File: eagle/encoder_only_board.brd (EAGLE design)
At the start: 34.5 x 29.1 mm, 27 parts, among them IC2 AT42QT1010SOT23, J1 FH12-6S-0.5SH(55), J2 FH12-6S-0.5SH(55)

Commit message: Update switch voltage divider and connect encoder touch to it
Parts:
- added R6: 0, rcl:R0603
- R24: value 0 -> 10k
- R4: value 10k -> 100k
- moved R4 16.3 mm to (26.2, 2.51), turned to 270 degrees
- moved R3 12.2 mm to (24.2, 2.51)
- moved R1 4.06 mm to (14.0, 2.51)
- moved R2 4.06 mm to (9.93, 2.51)
- moved R23 4.06 mm to (22.1, 2.51)
- moved R27 4.06 mm to (18.1, 2.51)
- moved R28 4.06 mm to (20.1, 2.51)
- moved R36 4.06 mm to (16.0, 2.51)
- moved R5 4.06 mm to (12.0, 2.51)
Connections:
- removed net N$2: R2.2, R3.2, R4.1
- removed net SW1: J1.1, J2.6, R24.2, R27.2, R28.2
- new net SW_IN: J1.1, R27.2, R28.2, R6.1
- new net SW_OUT: J2.6, R3.2
- net ENC_SW: now also R3.1, R4.1
- net ENC_SW_PU: now also R24.2, R6.2; no longer R3.1
- net GND: now also R2.2
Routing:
- net SW1: track 69.6 -> 0.00 mm, vias 4 -> 0
- net SW_IN: track 0.00 -> 47.0 mm, vias 0 -> 3
- net SW_OUT: track 0.00 -> 15.1 mm
- net ENC_SW: track 5.72 -> 10.0 mm
- net N$2: track 4.06 -> 0.00 mm
- net VCC: track 98.0 -> 102.1 mm
- net POT+: track 6.83 -> 3.51 mm
- net ENC2B: track 47.6 -> 46.4 mm
- net POT: track 5.26 -> 4.43 mm
- net ENC2A: track 53.1 -> 52.4 mm
- net GND: vias 17 -> 26
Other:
- board text added: "E+T"
- board text added: "SWO"
- board text added: "v1.0.1"
- board text removed: "P+T"
- board text removed: "SW1,2"
- board text removed: "v1.0.0"

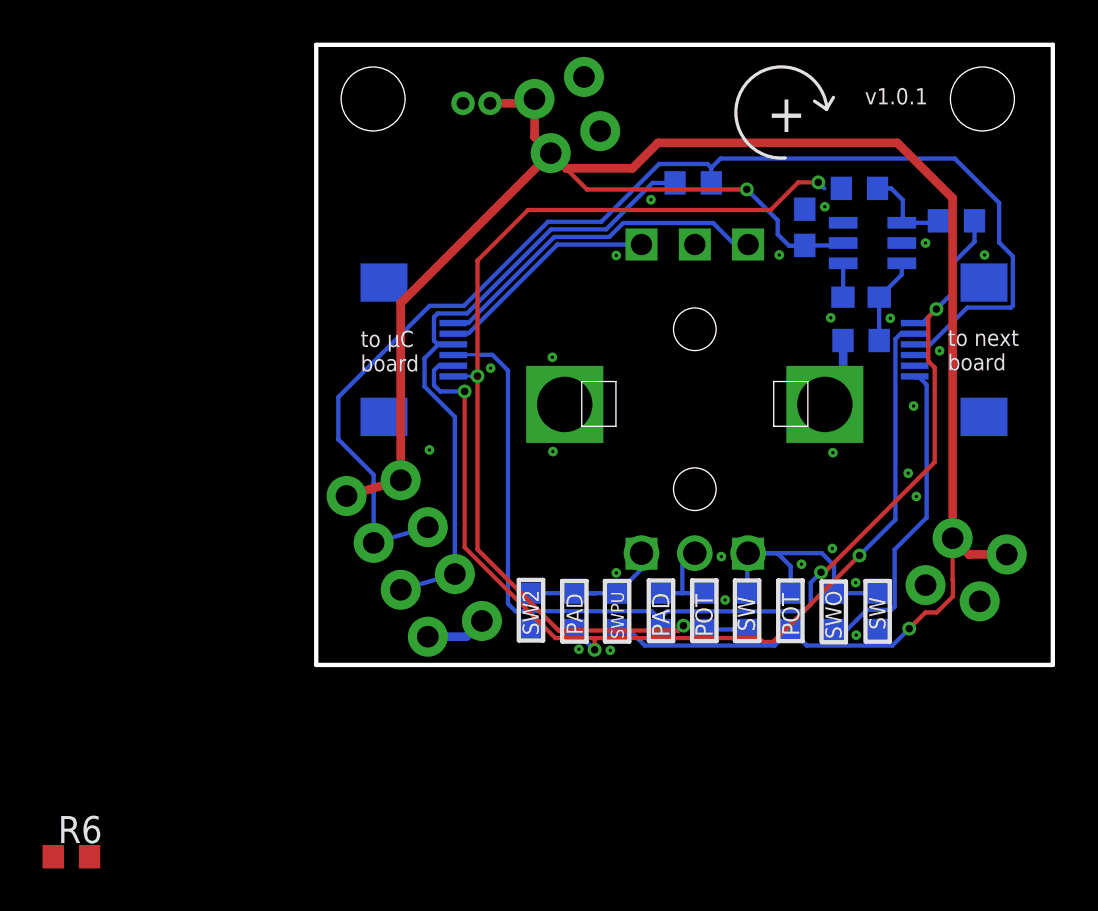
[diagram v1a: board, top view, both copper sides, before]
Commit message: Board version 4 WIP;
* Added solder pads to FFC connectors
* Fixed naming of connectors (previously M was on the right and labels
  were wrong
* Flipped builtin led (D1) around to make it safer to use with encoders
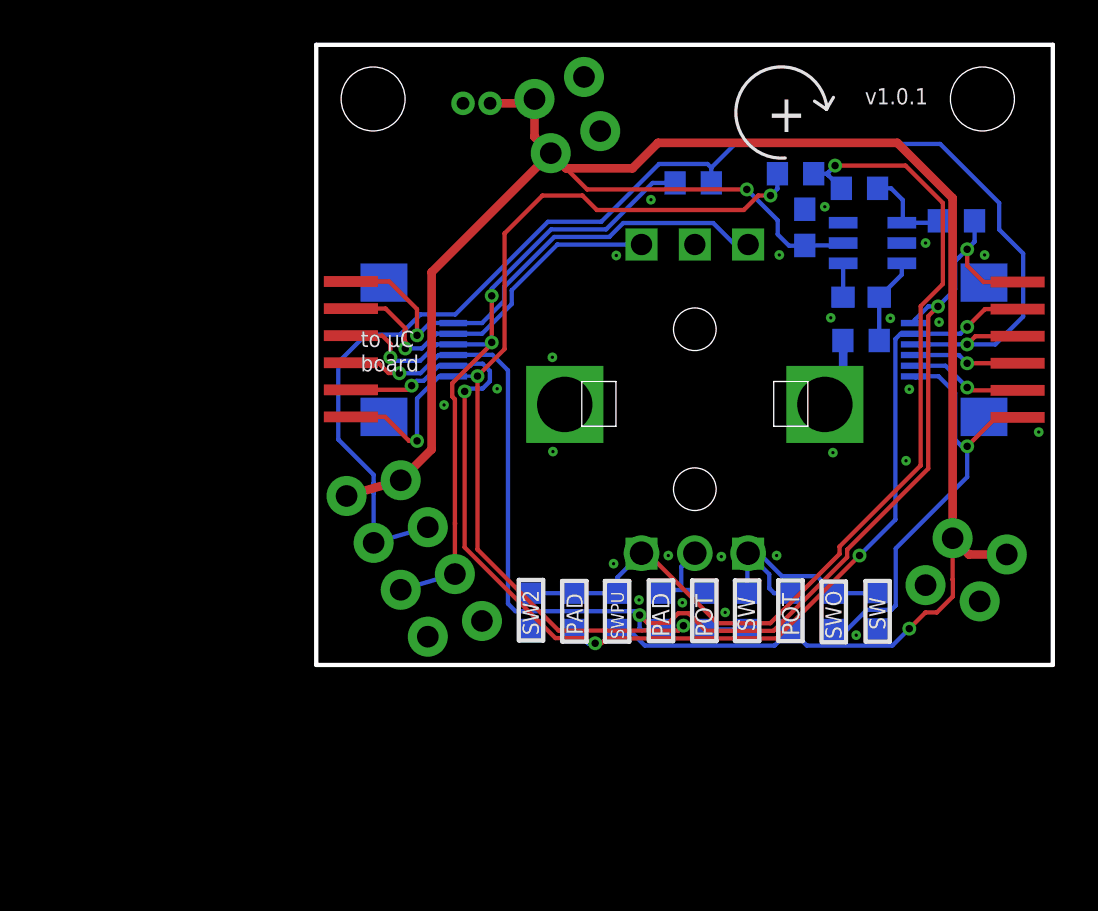
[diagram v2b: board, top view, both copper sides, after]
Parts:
- added U$1, U$2: 6PIN_SOLDER_PAD, edge:6PIN_SOLDER_PAD
- moved R6 46.7 mm to (22.4, 23.0), flipped to the bottom, turned to 180 degrees
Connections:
- removed net N$10: J2.4
- removed net N$14: J2.5
- new net NC1: J2.4, U$1.P$4
- new net NC2: J2.5, U$1.P$5
- net ENC1A: now also U$2.P$6
- net ENC1B: now also U$2.P$5
- net ENC2A: now also U$1.P$1, U$2.P$3
- net ENC2B: now also U$1.P$2, U$2.P$2
- net LED_IN: now also U$2.P$4
- net LED_OUT: now also U$1.P$3
- net SW_IN: now also U$2.P$1
- net SW_OUT: now also U$1.P$6
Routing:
- net ENC_SW_PU: track 7.48 -> 44.8 mm, vias 0 -> 1
- net ENC2B: track 46.4 -> 56.9 mm, vias 3 -> 5
- net ENC2A: track 52.4 -> 62.3 mm, vias 2 -> 4
- net ENC1A: track 16.2 -> 23.4 mm, vias 0 -> 1
- net ENC1B: track 10.6 -> 17.4 mm, vias 0 -> 1
- net SW_IN: track 47.0 -> 53.5 mm, vias 3 -> 4
- net NC2: track 0.00 -> 5.30 mm, vias 0 -> 1
- net SW_OUT: track 15.1 -> 20.3 mm, vias 0 -> 1
- net LED_OUT: track 58.0 -> 63.0 mm, vias 0 -> 1
- net LED_IN: track 30.3 -> 35.3 mm, vias 0 -> 3
- net NC1: track 0.00 -> 4.99 mm, vias 0 -> 1
- net GND: track 2.85 -> 0.00 mm, vias 26 -> 25
- net ENC_SW: track 10.0 -> 8.68 mm
